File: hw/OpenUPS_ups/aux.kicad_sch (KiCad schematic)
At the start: 8 parts, among them U801 NCP431, U802 LM317LCPK

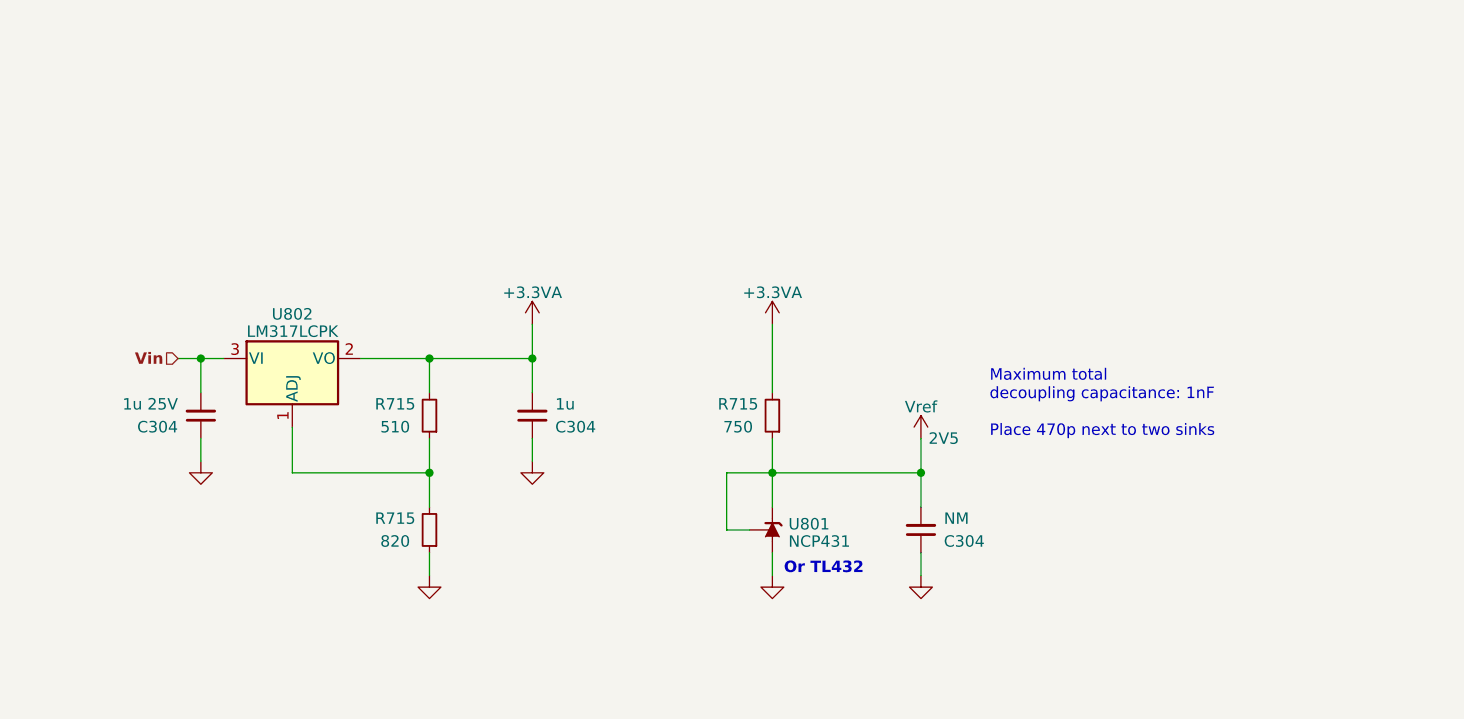
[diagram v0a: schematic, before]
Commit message: Upgraded battery charger with synchronous HB Driver
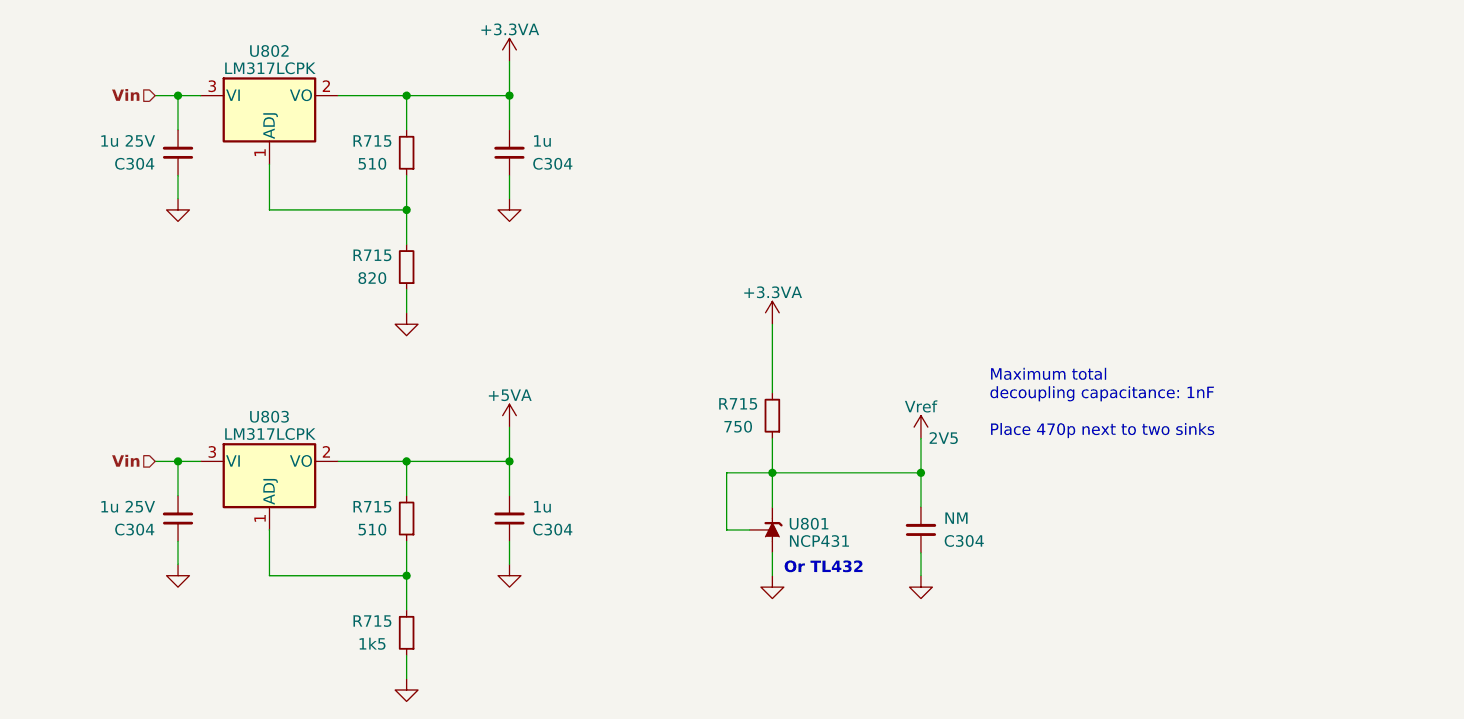
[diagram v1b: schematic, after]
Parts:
- added C304: 1u, Capacitor_SMD:C_0603_1608Metric, symbol Device:C_Small
- added C304: 1u 25V, Capacitor_SMD:C_0603_1608Metric, symbol Device:C_Small
- added R715: 510, Resistor_SMD:R_0603_1608Metric, symbol Device:R_Small
- added R715: 1k5, Resistor_SMD:R_0603_1608Metric, symbol Device:R_Small
- added U803: LM317LCPK, Package_TO_SOT_SMD:SOT-89-3, symbol Regulator_Linear:LM317L_SOT-89
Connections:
- net GND: now also C304.1, C304.1, R715.1
- net Vin: now also C304.2, U803.3 (VI)
- new net: R715.1, R715.2, U803.1 (ADJ)
- new net +5VA: C304.2, R715.2, U803.2 (VO)
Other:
- moved on the sheet: C304, R715, U802

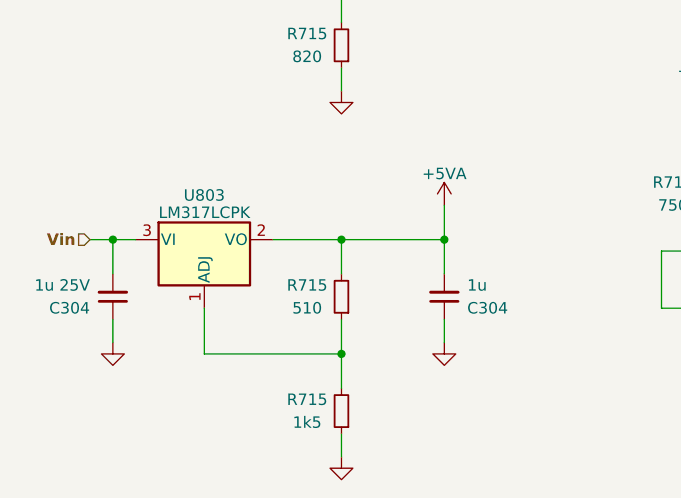
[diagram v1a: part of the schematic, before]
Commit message: Battery charger HB driver changed to NCP5901
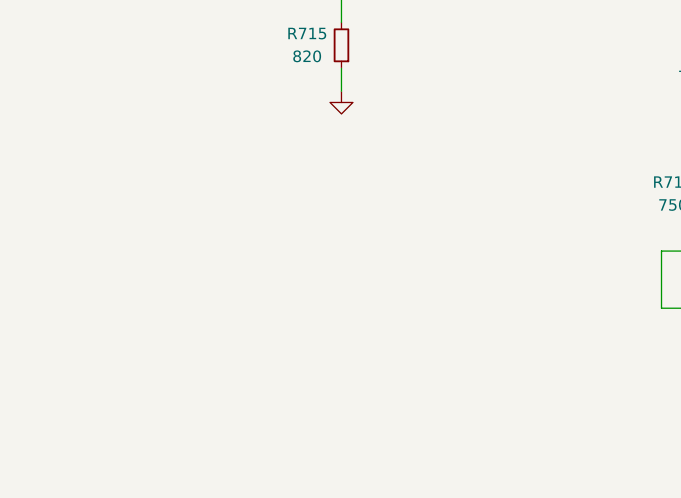
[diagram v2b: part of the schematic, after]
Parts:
- removed C304: 1u, Capacitor_SMD:C_0603_1608Metric, symbol Device:C_Small
- removed C304: 1u 25V, Capacitor_SMD:C_0603_1608Metric, symbol Device:C_Small
- removed R715: 510, Resistor_SMD:R_0603_1608Metric, symbol Device:R_Small
- removed R715: 1k5, Resistor_SMD:R_0603_1608Metric, symbol Device:R_Small
- removed U803: LM317LCPK, Package_TO_SOT_SMD:SOT-89-3, symbol Regulator_Linear:LM317L_SOT-89

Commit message: Work on Buck Boosts
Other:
- moved on the sheet: C304, R715, U801

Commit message: Issue #17
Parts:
- removed R715: 510, Resistor_SMD:R_0603_1608Metric, symbol Device:R_Small
- removed R715: 820, Resistor_SMD:R_0603_1608Metric, symbol Device:R_Small
- removed U802: LM317LCPK, Package_TO_SOT_SMD:SOT-89-3, symbol Regulator_Linear:LM317L_SOT-89
- added D801: BAT54C, Package_TO_SOT_SMD:SOT-23, symbol Diode:BAT54C
- added R715: 10k, Resistor_SMD:R_0603_1608Metric, symbol Device:R_Small
- added U803: AP7383-33W5, Package_TO_SOT_SMD:SOT-23-5, symbol OpenUPS_ups:AP3783-xxxW5
- U801: Alt (none) -> TL432
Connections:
- net +3.3VA: now also U803.5 (VOUT)
- net GND: now also R715.1, U803.2 (GND), U803.4 (NC)
- net Vin: now also U803.1 (VIN)
- new net: D801.3, R715.2, U803.3 (EN)
- new net EN1: D801.2
- new net EN2: D801.1
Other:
- note added: "Positive OR 30V tolerant 2.7V threshold"
- note removed: "Or TL432"
- moved on the sheet: C304, R715, U801

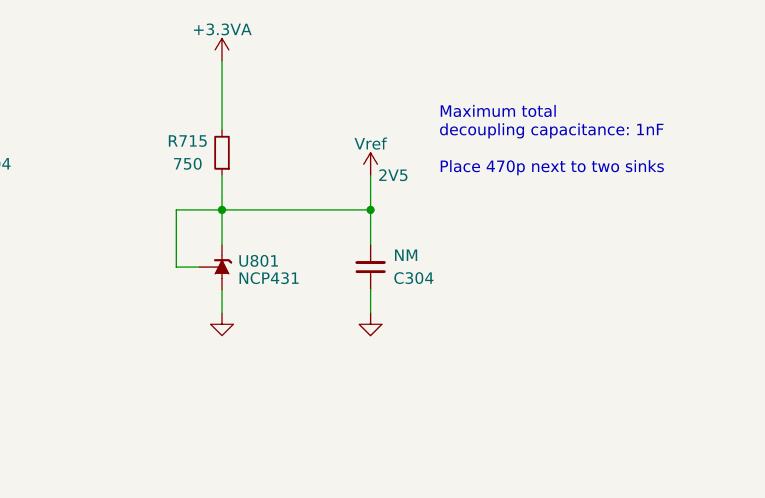
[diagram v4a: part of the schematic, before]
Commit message: Removed Vref (AVR has its own). Replaced INA181s with INA180s
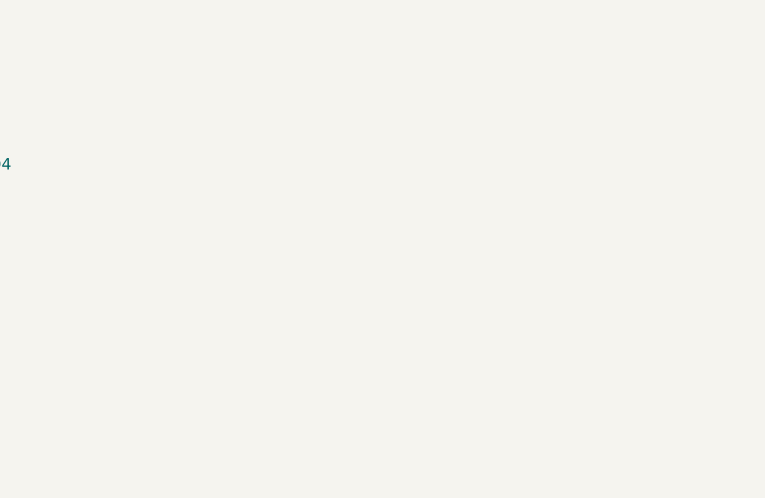
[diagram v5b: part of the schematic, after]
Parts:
- removed C304: NM, Capacitor_SMD:C_0603_1608Metric, symbol Device:C_Small
- removed R715: 750, Resistor_SMD:R_0603_1608Metric, symbol Device:R_Small
- removed U801: NCP431, Package_TO_SOT_SMD:SOT-23, symbol Reference_Voltage:TL432DBZ
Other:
- note removed: "Maximum total decoupling capacitance: 1nF Place 470p next to two sinks"

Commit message: Initial placement effort
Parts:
- renumbered U803 to U801
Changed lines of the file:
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@@
         )
         (path "/f77faec3-eac4-47f3-a2de-ec4a039f4502/8c312927-9c4e-41ad-b941-6f477a792759"
-          (reference "#PWR0809") (unit 1)
+          (reference "#PWR0804") (unit 1)
         )
       )
@@
         )
         (path "/f77faec3-eac4-47f3-a2de-ec4a039f4502/8c312927-9c4e-41ad-b941-6f477a792759"
-          (reference "R802") (unit 1)
+          (reference "R801") (unit 1)
         )
       )
@@
         )
         (path "/f77faec3-eac4-47f3-a2de-ec4a039f4502/8c312927-9c4e-41ad-b941-6f477a792759"
-          (reference "#PWR0810") (unit 1)
+          (reference "#PWR0802") (unit 1)
         )
       )
@@
         )
         (path "/f77faec3-eac4-47f3-a2de-ec4a039f4502/8c312927-9c4e-41ad-b941-6f477a792759"
-          (reference "C803") (unit 1)
+          (reference "C801") (unit 1)
         )
       )
@@
         )
         (path "/f77faec3-eac4-47f3-a2de-ec4a039f4502/8c312927-9c4e-41ad-b941-6f477a792759"
-          (reference "#PWR0801") (unit 1)
+          (reference "#PWR0805") (unit 1)
         )
       )
@@
         )
         (path "/f77faec3-eac4-47f3-a2de-ec4a039f4502/8c312927-9c4e-41ad-b941-6f477a792759"
-          (reference "#PWR0806") (unit 1)
+          (reference "#PWR0803") (unit 1)
         )
       )
@@
   (symbol (lib_id "OpenUPS_ups:AP3783-xxxW5") (at 73.66 25.4 0) (unit 1)
     (in_bom yes) (on_board yes) (dnp no) (fields_autoplaced)
-    (property "Reference" "U803" (at 73.66 22.3901 0)
+    (property "Reference" "U801" (at 73.66 22.3901 0)
       (effects (font (size 1.27 1.27)))
     )
@@
       (project "OpenUPS_ups"
         (path "/f77faec3-eac4-47f3-a2de-ec4a039f4502/8c312927-9c4e-41ad-b941-6f477a792759"
-          (reference "U803") (unit 1)
+          (reference "U801") (unit 1)
         )
       )
@@
         )
         (path "/f77faec3-eac4-47f3-a2de-ec4a039f4502/8c312927-9c4e-41ad-b941-6f477a792759"
-          (reference "#PWR0807") (unit 1)
+          (reference "#PWR0806") (unit 1)
         )
       )
@@
         )
         (path "/f77faec3-eac4-47f3-a2de-ec4a039f4502/8c312927-9c4e-41ad-b941-6f477a792759"
-          (reference "#PWR0808") (unit 1)
-        )
-      )
+          (reference "#PWR0801") (unit 1)
+        )
+      )
